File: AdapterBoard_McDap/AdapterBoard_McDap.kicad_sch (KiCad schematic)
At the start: 4 parts, among them J1 CN7, J2 CN10, J2_J4 LaunchPad, J3_J1 LaunchPad

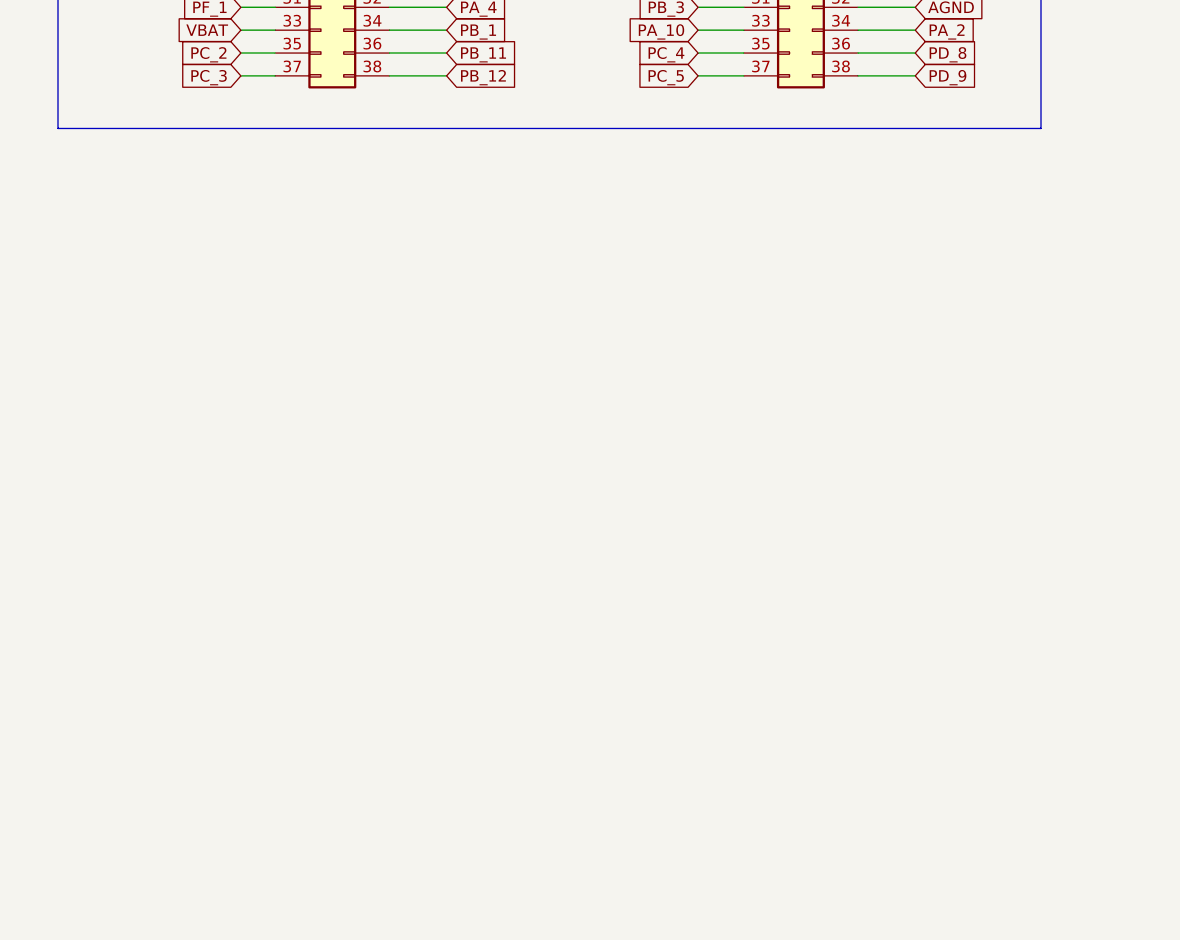
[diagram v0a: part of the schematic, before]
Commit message: Added pinmap connections to schematic; Finished layout for adapter board
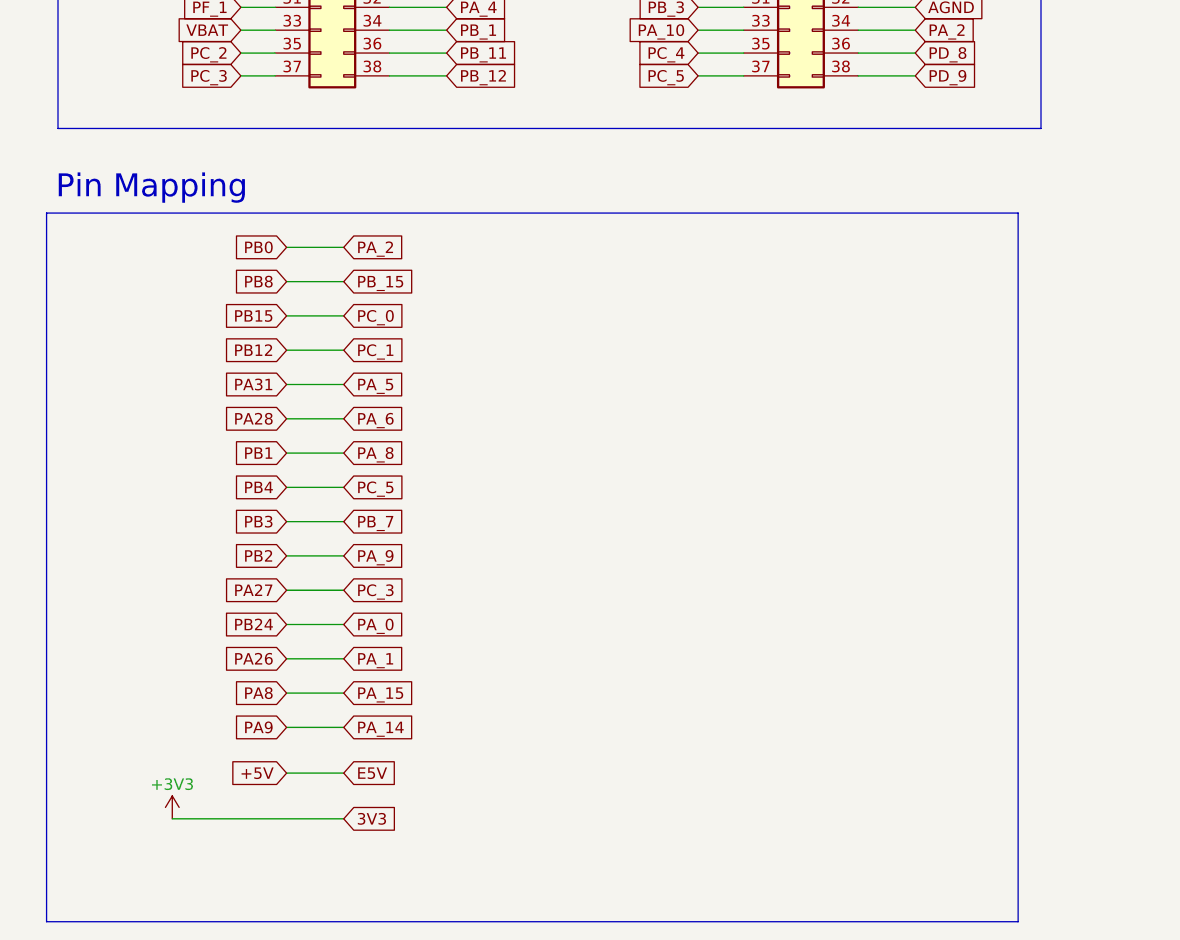
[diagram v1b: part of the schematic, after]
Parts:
- J2_J4, J3_J1: footprint RSLK2:LaunchPad -> Connector_PinHeader_2.54mm:PinHeader_2x10_P2.54mm_Vertical
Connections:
- net 3V3 is gone; now on net +3V3: J1.16 (Pin_16)
- net E5V is gone; now on net +5V: J1.6 (Pin_6)
- net PA_1 is gone; now on net PA26: J1.30 (Pin_30)
- net PA_14 is gone; now on net PA9: J1.7 (Pin_7)
- net PA_15 is gone; now on net PA8: J1.17 (Pin_17)
- net PA_5 is gone; now on net PA31: J2.11 (Pin_11)
- net PA_6 is gone; now on net PA28: J2.13 (Pin_13)
- net PB0 is gone; now on net PA_2: J2_J4.18
- net PB1 is gone; now on net PA_8: J2_J4.3
- net PB2 is gone; now on net PA_9: J3_J1.17
- net PB24 is gone; now on net PA_0: J3_J1.11
- net PB_15 is gone; now on net PB8: J2.26 (Pin_26)
- net PB_7 is gone; now on net PB3: J1.21 (Pin_21)
- net PC_0 is gone; now on net PB15: J2.18 (Pin_18)
- net PC_1 is gone; now on net PB12: J2.16 (Pin_16)
- net PC_3 is gone; now on net PA27: J1.37 (Pin_37)
- net PC_5 is gone; now on net PB4: J2.37 (Pin_37)
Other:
- note added: "Pin Mapping"

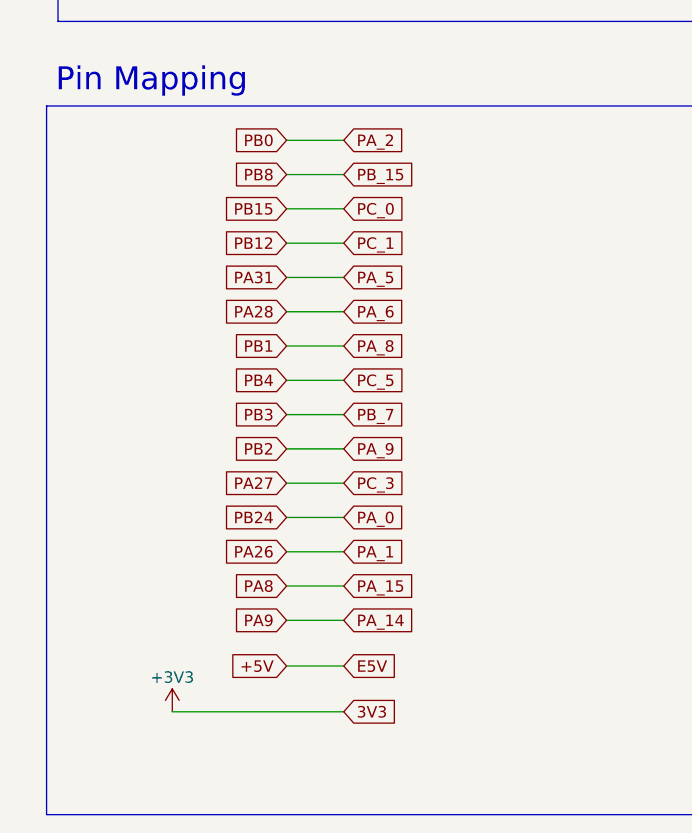
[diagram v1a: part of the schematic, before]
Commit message: Add missing pin connection between TI and STM
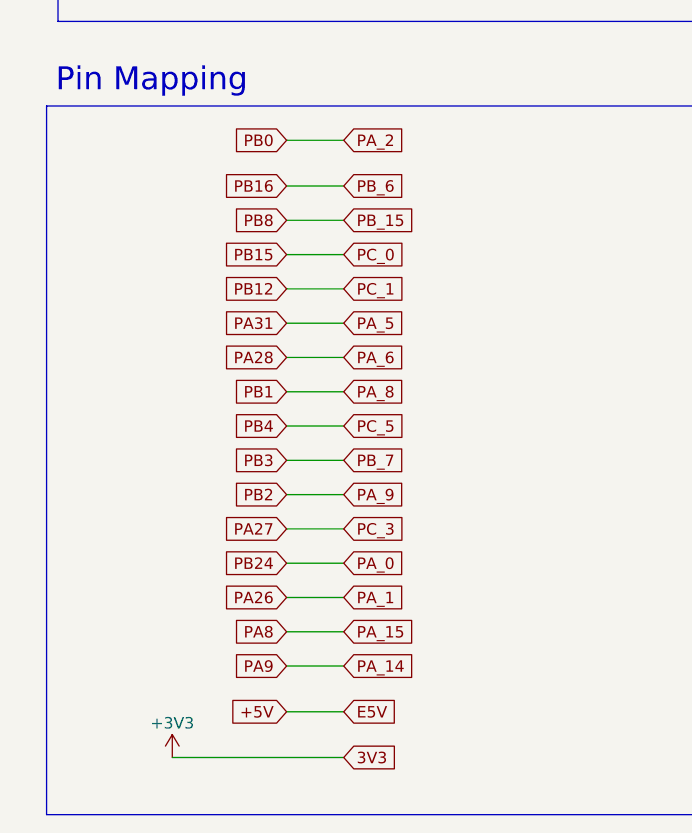
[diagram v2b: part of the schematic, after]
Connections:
- net PB_6 is gone; now on net PB16: J2.24 (Pin_24)

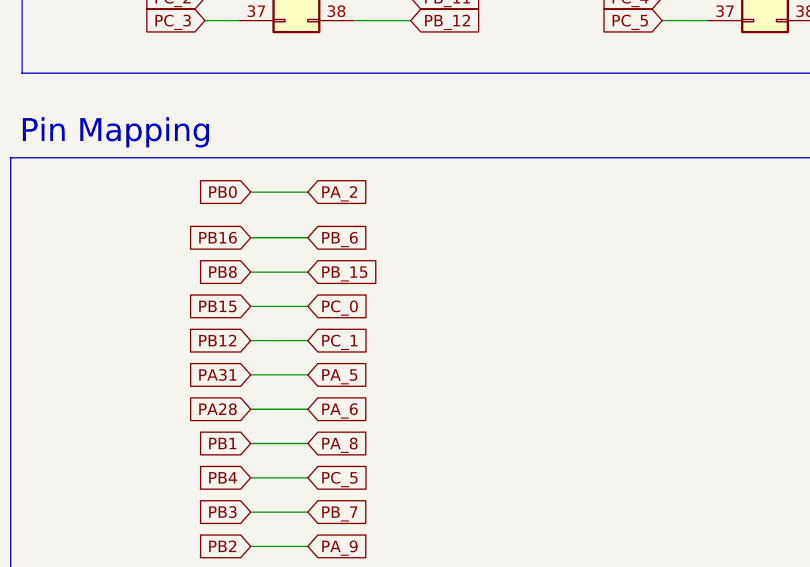
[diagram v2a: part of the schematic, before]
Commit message: changed pin mappings
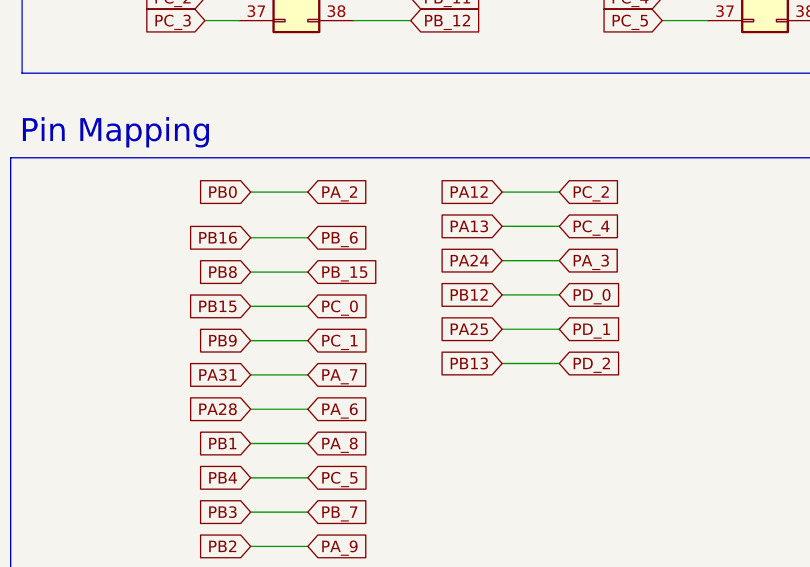
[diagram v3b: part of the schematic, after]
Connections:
- net PA_3 is gone; now on net PA24: J2.6 (Pin_6)
- net PA_7 is gone; now on net PA31: J2.15 (Pin_15)
- net PC_2 is gone; now on net PA12: J1.35 (Pin_35)
- net PC_4 is gone; now on net PA13: J2.35 (Pin_35)
- net PD_0 is gone; now on net PB12: J1.9 (Pin_9)
- net PD_1 is gone; now on net PA25: J1.10 (Pin_10)
- net PD_2 is gone; now on net PB13: J1.4 (Pin_4)
- net PA31: no longer J2.11 (Pin_11)
- net PB12: no longer J2.16 (Pin_16)
- net PB9: now also J2.16 (Pin_16)
- new net PA_5: J2.11 (Pin_11)
